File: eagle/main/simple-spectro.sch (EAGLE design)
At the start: 46 parts, among them CON1 BAT, CON2 SPI, CON3 SPI, IC1 32U4, IC2 MCP73831T, IC3 MCP1703-33, IC4 DMP1045U, X1 8MHz, X2 MINI-USB

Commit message: towards final box
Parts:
- C4, C5, C6, C8: MPN 77-VJ1206V106MXQTBC -> 77-VJ1206V106ZXQTBC
- X1: MPN 520-8.0-18-23G-JGNT -> 729-F60800010
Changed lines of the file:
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@@
 </part>
 <part name="X1" library="lpatiny" deviceset="XTAL" device="NX6035" value="8MHz">
-<attribute name="MPN" value="520-8.0-18-23G-JGNT"/>
+<attribute name="MPN" value="729-F60800010"/>
 </part>
 <part name="SUPPLY6" library="supply1" deviceset="VCC" device=""/>
@@
 </part>
 <part name="C5" library="dp_devices" deviceset="CAPACITOR_NPOL" device="-1206" value="10u">
-<attribute name="MPN" value="77-VJ1206V106MXQTBC"/>
+<attribute name="MPN" value="77-VJ1206V106ZXQTBC"/>
 </part>
 <part name="U$3" library="microbuilder" deviceset="GND" device=""/>
 <part name="C4" library="dp_devices" deviceset="CAPACITOR_NPOL" device="-1206" value="10u">
-<attribute name="MPN" value="77-VJ1206V106MXQTBC"/>
+<attribute name="MPN" value="77-VJ1206V106ZXQTBC"/>
 </part>
 <part name="U$5" library="microbuilder" deviceset="GND" device=""/>
@@
 <part name="LCD" library="HD44780LCD" deviceset="LCD-HD44780" device="16X2-4-HOLES" technology="4-HOLES"/>
 <part name="C8" library="resistor" library_urn="urn:adsk.eagle:library:348" deviceset="C-EU" device="C1206" value="10u">
-<attribute name="MPN" value="77-VJ1206V106MXQTBC"/>
+<attribute name="MPN" value="77-VJ1206V106ZXQTBC"/>
 </part>
 <part name="GND19" library="supply1" deviceset="GND" device=""/>
 <part name="C6" library="resistor" library_urn="urn:adsk.eagle:library:348" deviceset="C-EU" device="C1206" value="10u">
-<attribute name="MPN" value="77-VJ1206V106MXQTBC"/>
+<attribute name="MPN" value="77-VJ1206V106ZXQTBC"/>
 </part>
 <part name="IC3" library="linear" deviceset="MCP1703" device="DB" value="MCP1703-33">

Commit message: update box
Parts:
- C1, C2: LCSC (none) -> C1889
- C10, C3, C7, C9: LCSC (none) -> C77502
- C4, C5, C6, C8: LCSC (none) -> C92789
- LED1: LCSC (none) -> C49018
- LED2: LCSC (none) -> C14641
- LED3: LCSC (none) -> C84273
- R1, R14, R2, R7, R8, R9: LCSC (none) -> C1469
- R13: LCSC (none) -> C1489
- R4, R5: LCSC (none) -> C99734
- R6: LCSC (none) -> C4410
- X1: LCSC (none) -> C90881

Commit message: update bom
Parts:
- C10, C3, C7, C9: ELECROW (none) -> C24497
- C4, C5, C6, C8: ELECROW (none) -> C13585
- D1, D2, D3: device lpatiny:1N581D1206 -> diode:MBR0520LT; LCSC (none) -> C82544; MPN 579-MCP1703-3302E/DB -> 621-1N5819HW-F
- IC1: LCSC (none) -> C44854
- IC2: LCSC (none) -> C14879
- IC3: LCSC (none) -> C50754
- IC4: value DMP1045U -> DMP1045U or DMG2302; LCSC (none) -> C96613
- R1, R14, R2, R7, R8, R9: ELECROW (none) -> C4410
- R11, R15: ELECROW (none) -> C17900
- R13: ELECROW (none) -> C17902; LCSC C1489 -> C17902
- R3: ELECROW (none) -> C17902; LCSC (none) -> C17902
- R4, R5: ELECROW (none) -> C17958

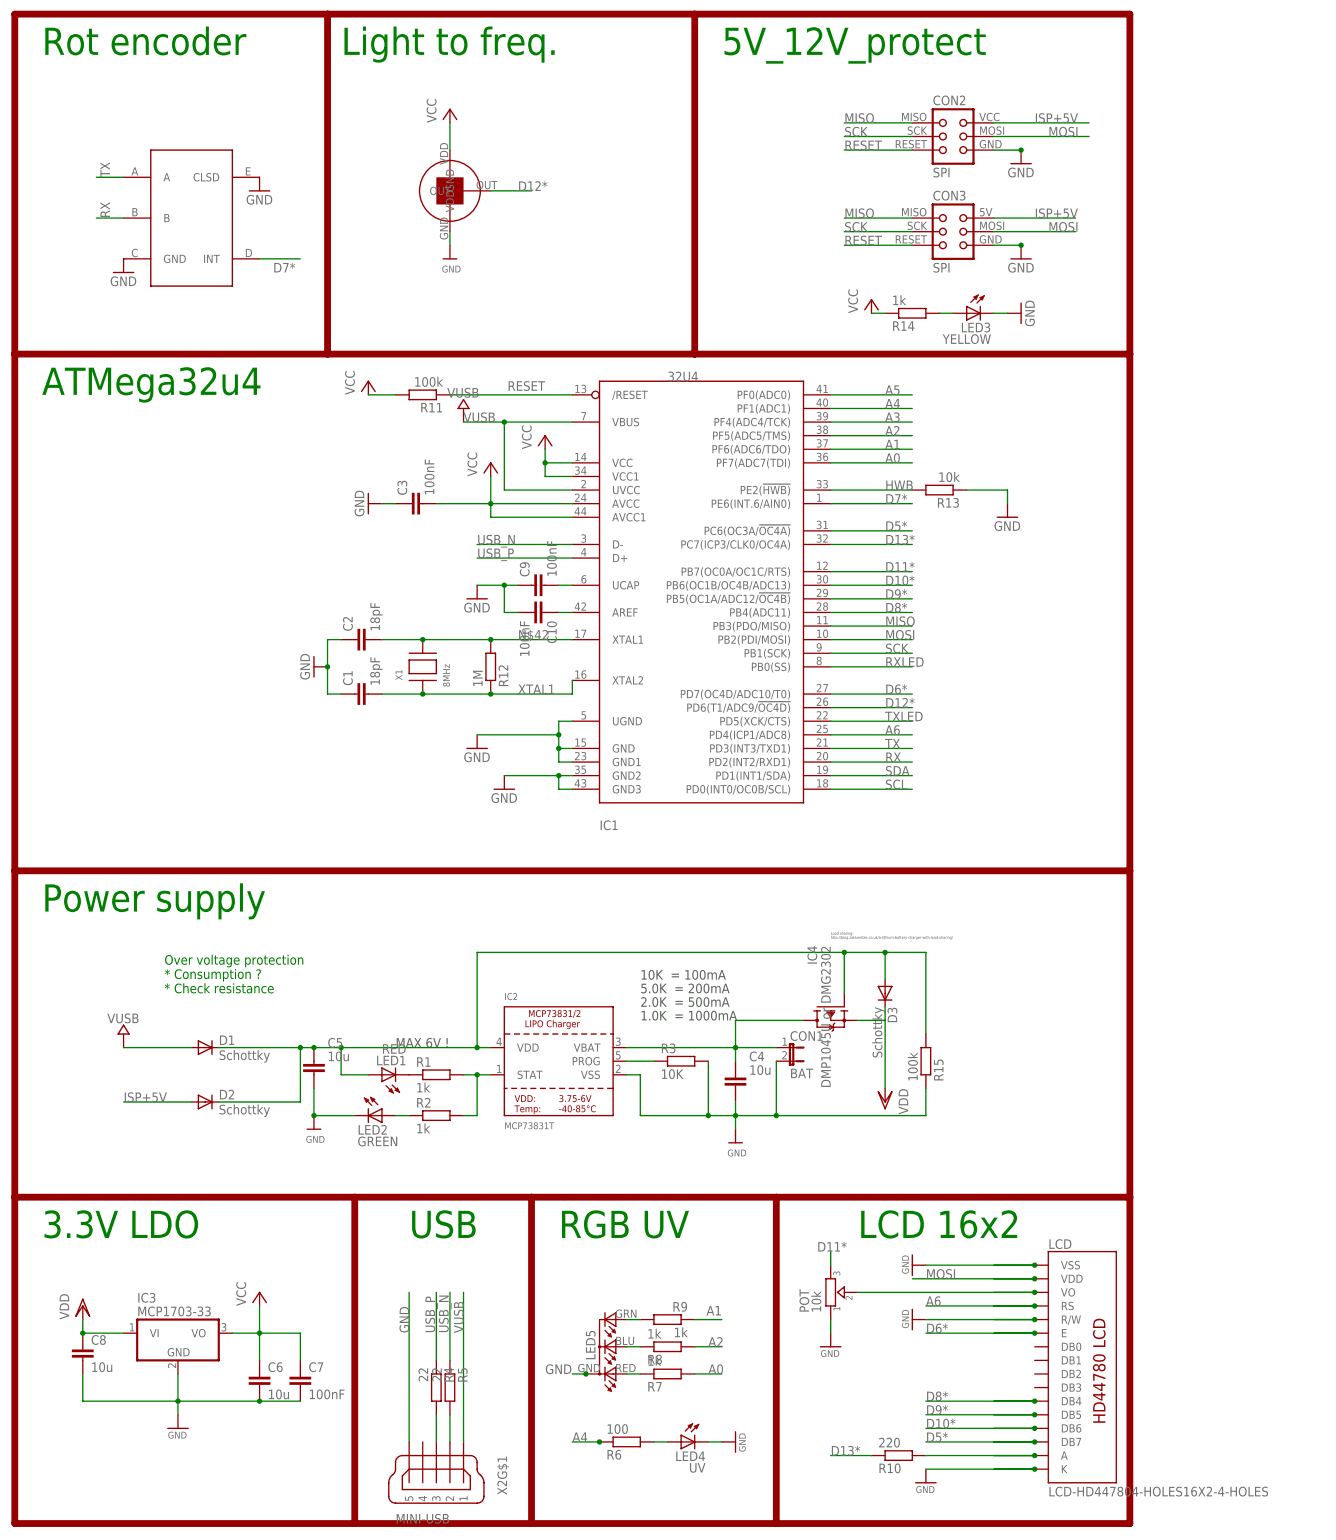
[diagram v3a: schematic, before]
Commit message: add battery monitoring
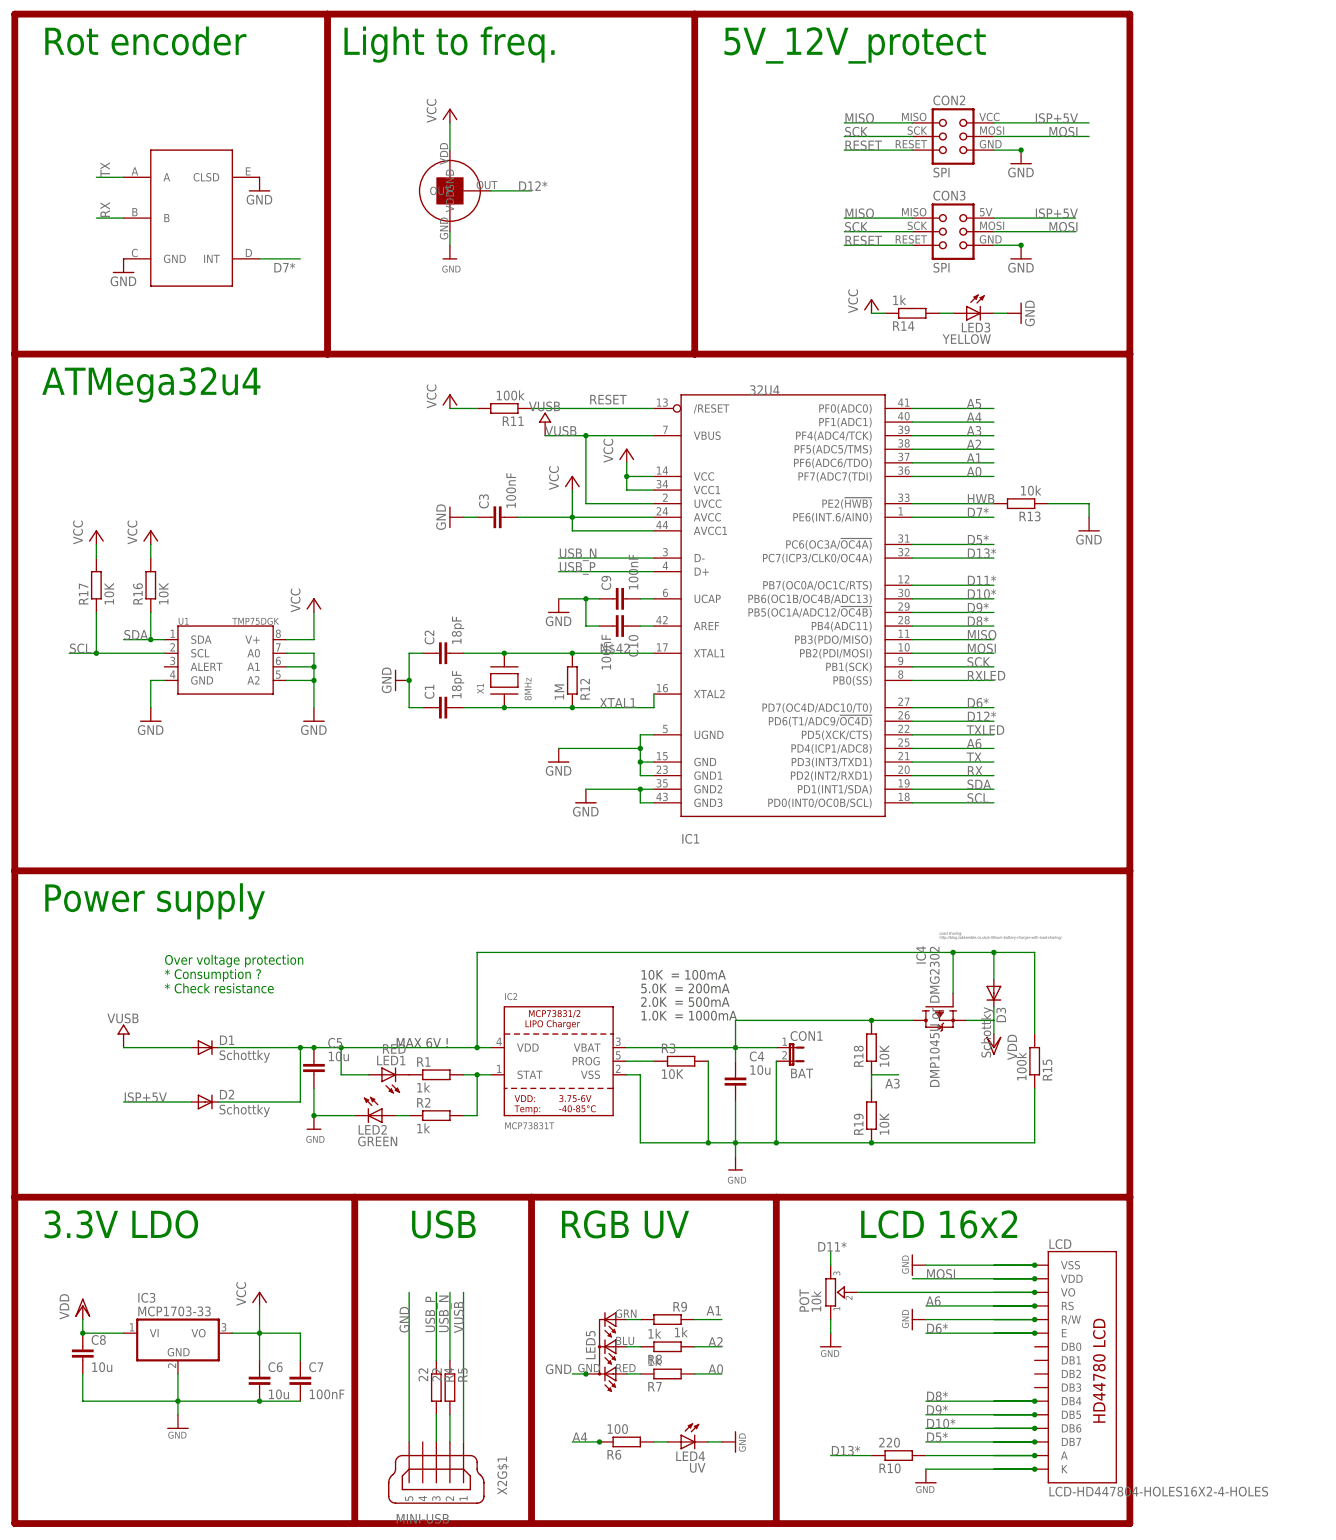
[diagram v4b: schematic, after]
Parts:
- added R16, R17, R18, R19: 10K, rcl:R-EU_M1206
- added U1: TMP75DGK, ti_tmp:TMP75DGK
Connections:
- net A3: now also R18.1, R19.2
- net GND: now also R19.1, U1.A0, U1.A1, U1.A2, U1.GND
- net SCL: now also R17.1, U1.SCL
- net SDA: now also R16.1, U1.SDA
- net VBAT1: now also R18.2
- net VCC: now also R16.2, R17.2, U1.V+
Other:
- moved on the sheet: C1, C10, C2, C3, C9, D3, IC1, IC4, R11, R12, R13, R15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

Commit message: working on vibration
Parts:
- added CON4: VIBR, jumper:JP1E
- added R20: 1k, rcl:R-EU_M1206
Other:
- note added: "Temperature"
- note added: "Vibrate"
- moved on the sheet: C1, C10, C2, C3, C9, IC1, LED3, R11, R12, R13, R14, R16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

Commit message: working on vibration
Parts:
- added Q6: BSP75, infineon:BSP613P
- R10: LCSC (none) -> C102128
- R11, R15: LCSC (none) -> C17900
- R12: ELECROW (none) -> C26124
- R16, R17, R18, R19: ELECROW (none) -> C17900; LCSC (none) -> C17900
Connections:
- new net N$14: CON4.2, Q6.D@1
- new net N$8: Q6.G, R20.2
- net A5: now also R20.1
- net GND: now also Q6.S
- net VCC: now also CON4.1
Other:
- moved on the sheet: CON4, R20
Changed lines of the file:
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@@
 <part name="GND54" library="supply1" deviceset="GND" device=""/>
 <part name="R12" library="rcl" library_urn="urn:adsk.eagle:library:334" deviceset="R-EU_" device="M1206" value="1M">
-<attribute name="ELECROW" value=""/>
+<attribute name="ELECROW" value="C26124"/>
 <attribute name="MPN" value="ERJ-8GEYJ105V"/>
 </part>
@@
 <part name="R10" library="rcl" deviceset="R-EU_" device="M1206" value="220">
 <attribute name="ELECROW" value=""/>
-<attribute name="LCSC" value=""/>
+<attribute name="LCSC" value="C102128"/>
 <attribute name="MPN" value="667-ERJ-U08J221V"/>
 </part>
@@
 <part name="R15" library="rcl" deviceset="R-EU_" device="M1206" value="100k">
 <attribute name="ELECROW" value="C17900"/>
-<attribute name="LCSC" value=""/>
+<attribute name="LCSC" value="C17900"/>
 <attribute name="MPN" value="RC1206FR-07100KL"/>
 </part>
@@
 <part name="R11" library="rcl" library_urn="urn:adsk.eagle:library:334" deviceset="R-EU_" device="M1206" value="100k">
 <attribute name="ELECROW" value="C17900"/>
-<attribute name="LCSC" value=""/>
+<attribute name="LCSC" value="C17900"/>
 <attribute name="MPN" value="RC1206FR-07100KL"/>
 </part>
@@
 <part name="GND10" library="supply1" deviceset="GND" device=""/>
 <part name="R16" library="rcl" deviceset="R-EU_" device="M1206" value="10K">
+<attribute name="ELECROW" value="C17900"/>
+<attribute name="LCSC" value="C17900"/>
 <attribute name="MPN" value="603-RC1206FR-0710KL"/>
 </part>
 <part name="R17" library="rcl" deviceset="R-EU_" device="M1206" value="10K">
+<attribute name="ELECROW" value="C17900"/>
+<attribute name="LCSC" value="C17900"/>
 <attribute name="MPN" value="603-RC1206FR-0710KL"/>
 </part>
@@
 <part name="SUPPLY9" library="supply1" deviceset="VCC" device=""/>
 <part name="R18" library="rcl" deviceset="R-EU_" device="M1206" value="10K">
+<attribute name="ELECROW" value="C17900"/>
+<attribute name="LCSC" value="C17900"/>
 <attribute name="MPN" value="603-RC1206FR-0710KL"/>
 </part>
 <part name="R19" library="rcl" deviceset="R-EU_" device="M1206" value="10K">
+<attribute name="ELECROW" value="C17900"/>
+<attribute name="LCSC" value="C17900"/>
 <attribute name="MPN" value="603-RC1206FR-0710KL"/>
 </part>
@@
 <attribute name="MPN" value="667-ERJ-8GEYJ101V"/>
 </part>
+<part name="Q6" library="infineon" deviceset="BSP613P" device="" value="BSP75"/>
+<part name="GND12" library="supply1" deviceset="GND" device=""/>
+<part name="SUPPLY10" library="supply1" deviceset="VCC" device=""/>
 </parts>
 <sheets>
@@
 <instance part="GND38" gate="1" x="93.98" y="177.8"/>
 <instance part="GND39" gate="1" x="63.5" y="165.1" rot="R270"/>
-<instance part="GND42" gate="1" x="93.98" y="149.86"/>
+<instance part="GND42" gate="1" x="93.98" y="149.86" rot="MR0"/>
 <instance part="GND45" gate="1" x="99.06" y="142.24"/>
 <instance part="GND54" gate="1" x="187.96" y="193.04"/>
@@
 <instance part="R16" gate="G$1" x="10.16" y="205.74" rot="R90">
 <attribute name="MPN" x="10.16" y="205.74" size="1.778" layer="96" rot="R90" display="off"/>
+<attribute name="LCSC" x="10.16" y="205.74" size="1.778" layer="96" rot="R90" display="off"/>
+<attribute name="ELECROW" x="10.16" y="205.74" size="1.778" layer="96" rot="R90" display="off"/>
 </instance>
 <instance part="R17" gate="G$1" x="0" y="205.74" rot="R90">
 <attribute name="MPN" x="0" y="205.74" size="1.778" layer="96" rot="R90" display="off"/>
+<attribute name="LCSC" x="0" y="205.74" size="1.778" layer="96" rot="R90" display="off"/>
+<attribute name="ELECROW" x="0" y="205.74" size="1.778" layer="96" rot="R90" display="off"/>
 </instance>
 <instance part="SUPPLY8" gate="VCC" x="10.16" y="215.9"/>
@@
 <instance part="R18" gate="G$1" x="144.78" y="96.52" rot="R90">
 <attribute name="MPN" x="144.78" y="96.52" size="1.778" layer="96" rot="R90" display="off"/>
+<attribute name="LCSC" x="144.78" y="96.52" size="1.778" layer="96" rot="R90" display="off"/>
+<attribute name="ELECROW" x="144.78" y="96.52" size="1.778" layer="96" rot="R90" display="off"/>
 </instance>
 <instance part="R19" gate="G$1" x="144.78" y="83.82" rot="R90">
 <attribute name="MPN" x="144.78" y="83.82" size="1.778" layer="96" rot="R90" display="off"/>
-</instance>
-<instance part="CON4" gate="A" x="30.48" y="147.32" rot="R270"/>
-<instance part="R20" gate="G$1" x="0" y="147.32">
-<attribute name="MPN" x="0" y="147.32" size="1.778" layer="96" display="off"/>
-<attribute name="LCSC" x="0" y="147.32" size="1.778" layer="96" display="off"/>
-<attribute name="ELECROW" x="0" y="147.32" size="1.778" layer="96" display="off"/>
-</instance>
+<attribute name="LCSC" x="144.78" y="83.82" size="1.778" layer="96" rot="R90" display="off"/>
+<attribute name="ELECROW" x="144.78" y="83.82" size="1.778" layer="96" rot="R90" display="off"/>
+</instance>
+<instance part="CON4" gate="A" x="33.02" y="157.48" rot="R270"/>
+<instance part="R20" gate="G$1" x="12.7" y="144.78">
+<attribute name="MPN" x="12.7" y="144.78" size="1.778" layer="96" display="off"/>
+<attribute name="LCSC" x="12.7" y="144.78" size="1.778" layer="96" display="off"/>
+<attribute name="ELECROW" x="12.7" y="144.78" size="1.778" layer="96" display="off"/>
+</instance>
+<instance part="Q6" gate="G$1" x="27.94" y="147.32"/>
+<instance part="GND12" gate="1" x="30.48" y="137.16" rot="MR0"/>
+<instance part="SUPPLY10" gate="VCC" x="30.48" y="162.56"/>
 </instances>
 <busses>
@@
 <wire x1="10.16" y1="187.96" x2="10.16" y2="182.88" width="0.1524" layer="91"/>
 </segment>
+<segment>
+<pinref part="Q6" gate="G$1" pin="S"/>
+<pinref part="GND12" gate="1" pin="GND"/>
+<wire x1="30.48" y1="142.24" x2="30.48" y2="139.7" width="0.1524" layer="91"/>
+</segment>
 </net>
 <net name="SCK" class="0">
@@
 <wire x1="160.02" y1="215.9" x2="175.26" y2="215.9" width="0.1524" layer="91"/>
 <label x="170.18" y="215.9" size="1.778" layer="95"/>
+</segment>
+<segment>
+<pinref part="R20" gate="G$1" pin="1"/>
+<wire x1="7.62" y1="144.78" x2="2.54" y2="144.78" width="0.1524" layer="91"/>
+<label x="2.54" y="144.78" size="1.778" layer="95"/>
 </segment>
 </net>
@@
 <wire x1="0" y1="210.82" x2="0" y2="213.36" width="0.1524" layer="91"/>
 <pinref part="SUPPLY9" gate="VCC" pin="VCC"/>
+</segment>
+<segment>
+<pinref part="SUPPLY10" gate="VCC" pin="VCC"/>
+<pinref part="CON4" gate="A" pin="1"/>
+<wire x1="30.48" y1="157.48" x2="30.48" y2="160.02" width="0.1524" layer="91"/>
 </segment>
 </net>
@@
 </segment>
 </net>
+<net name="N$8" class="0">
+<segment>
+<pinref part="R20" gate="G$1" pin="2"/>
+<pinref part="Q6" gate="G$1" pin="G"/>
+<wire x1="17.78" y1="144.78" x2="25.4" y2="144.78" width="0.1524" layer="91"/>
+</segment>
+</net>
+<net name="N$14" class="0">
+<segment>
+<pinref part="CON4" gate="A" pin="2"/>
+<pinref part="Q6" gate="G$1" pin="D@1"/>
+<wire x1="30.48" y1="154.94" x2="30.48" y2="152.4" width="0.1524" layer="91"/>
+</segment>
+</net>
